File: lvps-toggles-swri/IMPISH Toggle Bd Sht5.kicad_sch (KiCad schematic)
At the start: 22 parts, among them J7 BCS-105-L-D-TE, J8 BCS-105-L-D-TE, Q25 MMBT3904Q, Q26 MMBT3906Q, Q27 ZXM61N02F, U13 BSP742T, U14 BSP452

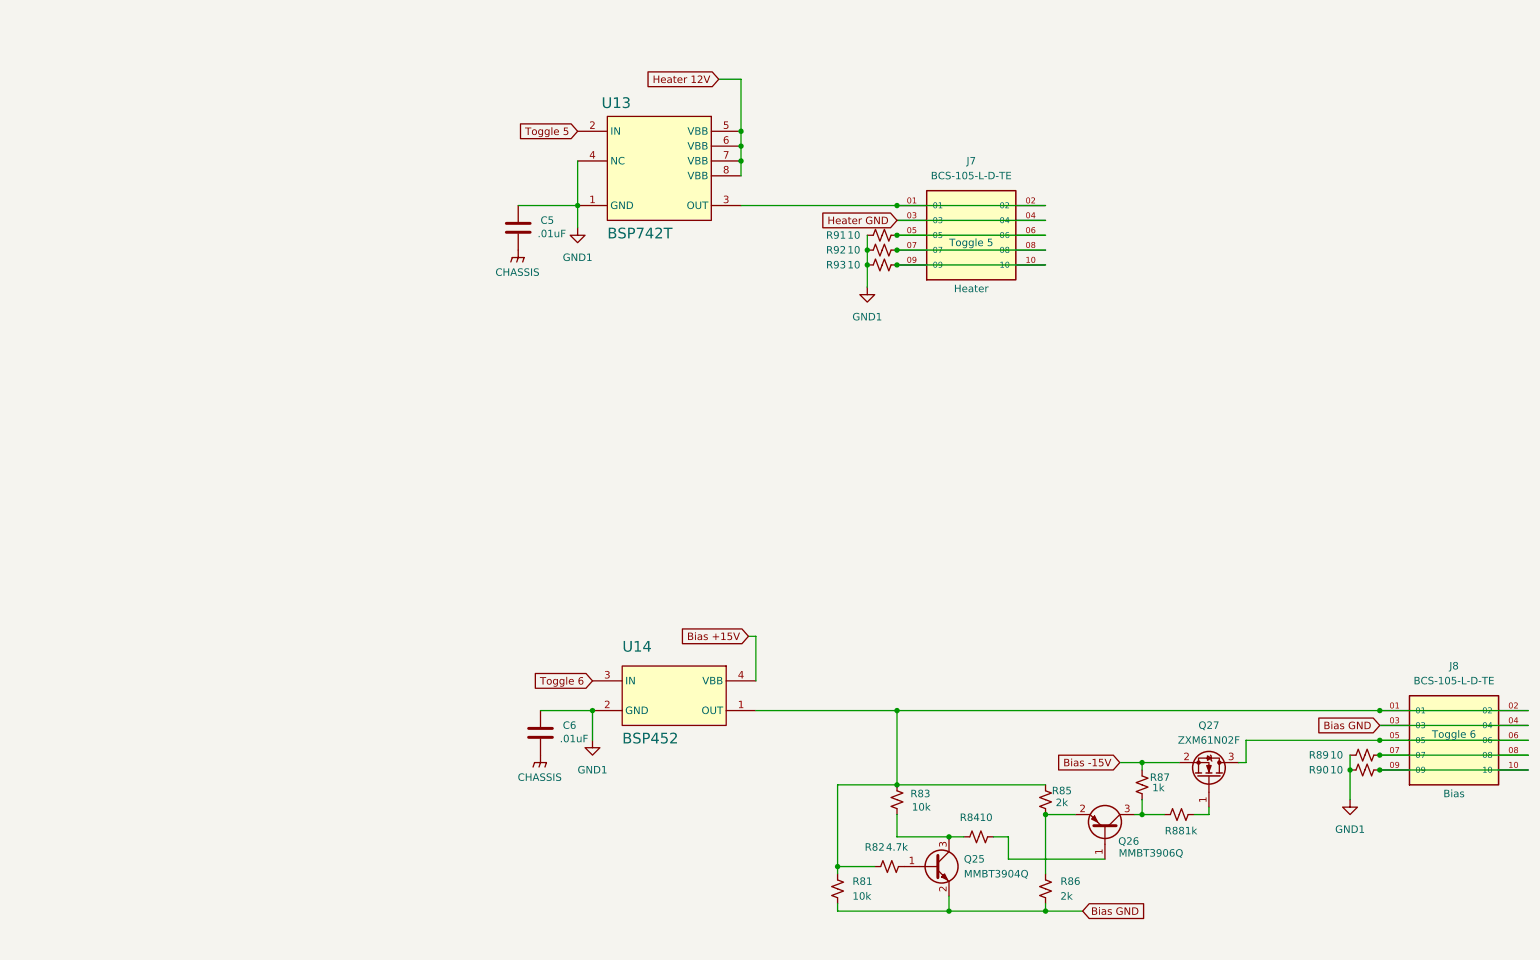
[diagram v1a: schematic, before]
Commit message: swri toggles: start one ground
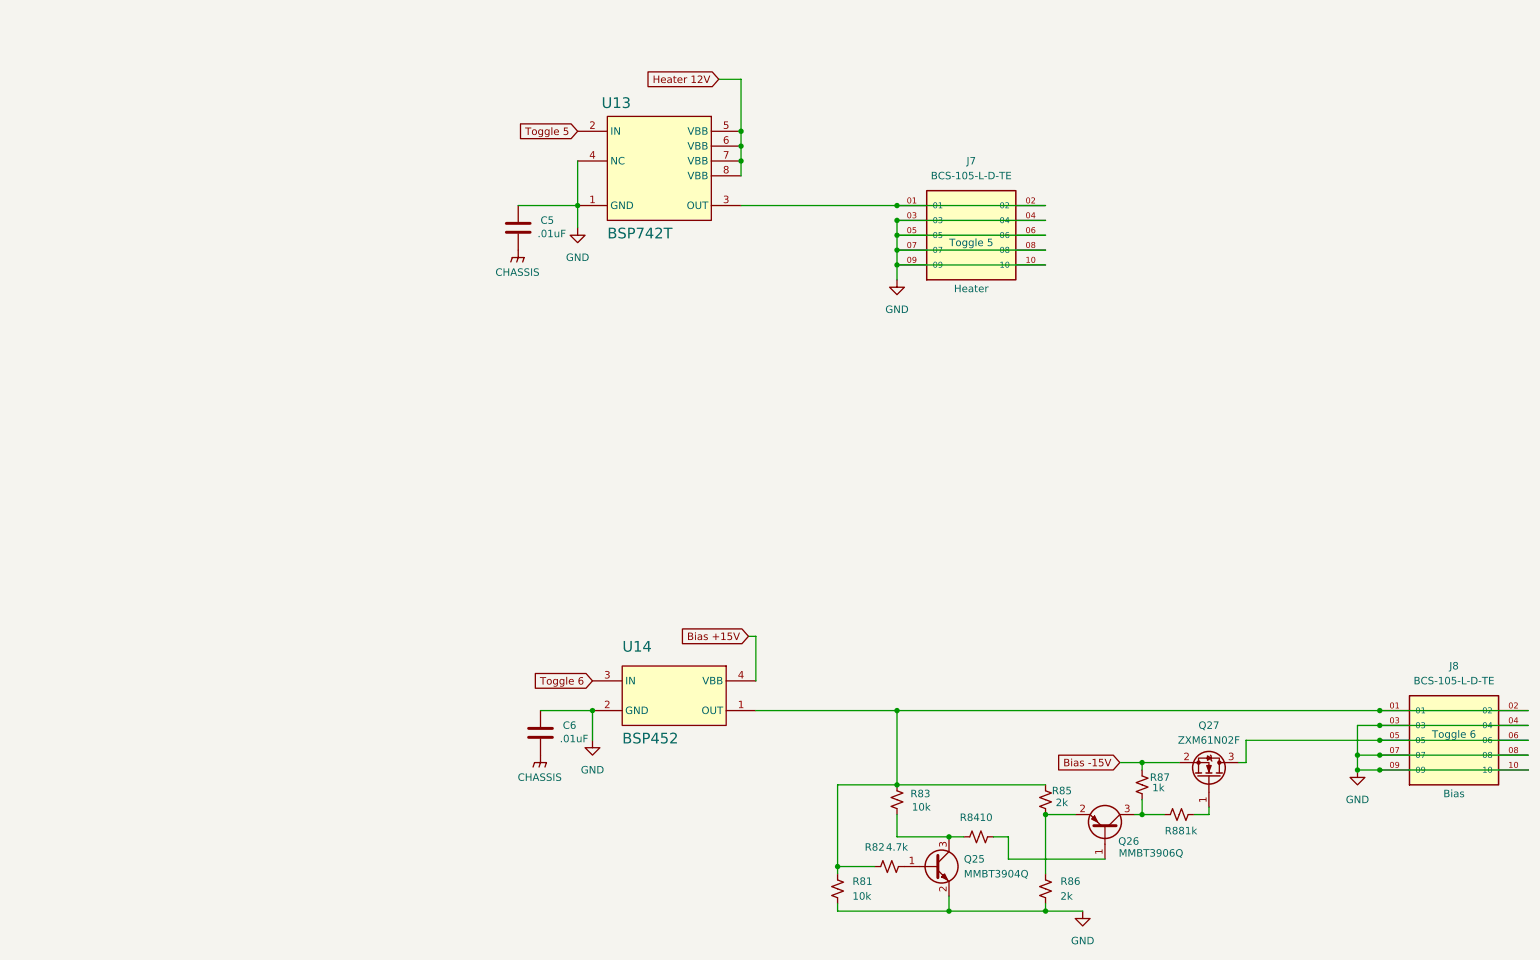
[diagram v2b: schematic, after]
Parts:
- removed R89, R90, R91, R92, R93: 10, Resistor_SMD:R_0805_2012Metric_Pad1.20x1.40mm_HandSolder, symbol Device:R_Small_US
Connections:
- net Bias GND is gone; now on net GND: J8.03, J8.04, Q25.2 (E), R81.2, R86.2
- net GND1 is gone; now on net GND: C5.2, C6.2, U13.1 (GND), U13.4 (NC), U14.2 (GND)
- net Heater GND is gone; now on net GND: J7.03, J7.04
- net GND: now reaches J8.09, J8.10
- net GND: now also J7.05, J7.06, J7.07, J7.08, J7.09, J7.10, J8.07, J8.08

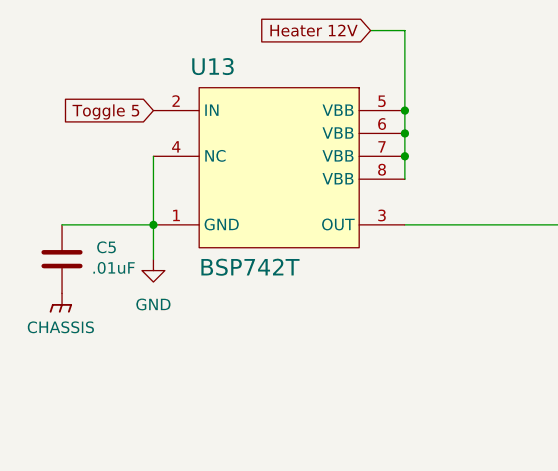
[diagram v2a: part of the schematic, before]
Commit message: swri: NC pin on toggle
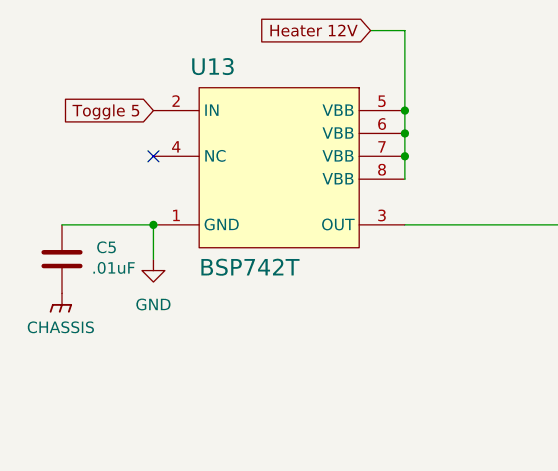
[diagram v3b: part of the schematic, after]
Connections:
- net GND: no longer U13.4 (NC)
- no-connect marks 0 -> 1
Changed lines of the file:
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@@
 		(color 0 0 0 0)
 	)
+	(no_connect
+		(at 118.11 68.58)
+	)
 	(wire
 		(pts
@@
 		)
 		(stroke
-			(width 0)
-			(type default)
-		)
-	)
-	(wire
-		(pts
-			(xy 118.11 68.58) (xy 118.11 76.2)
-		)
-		(stroke

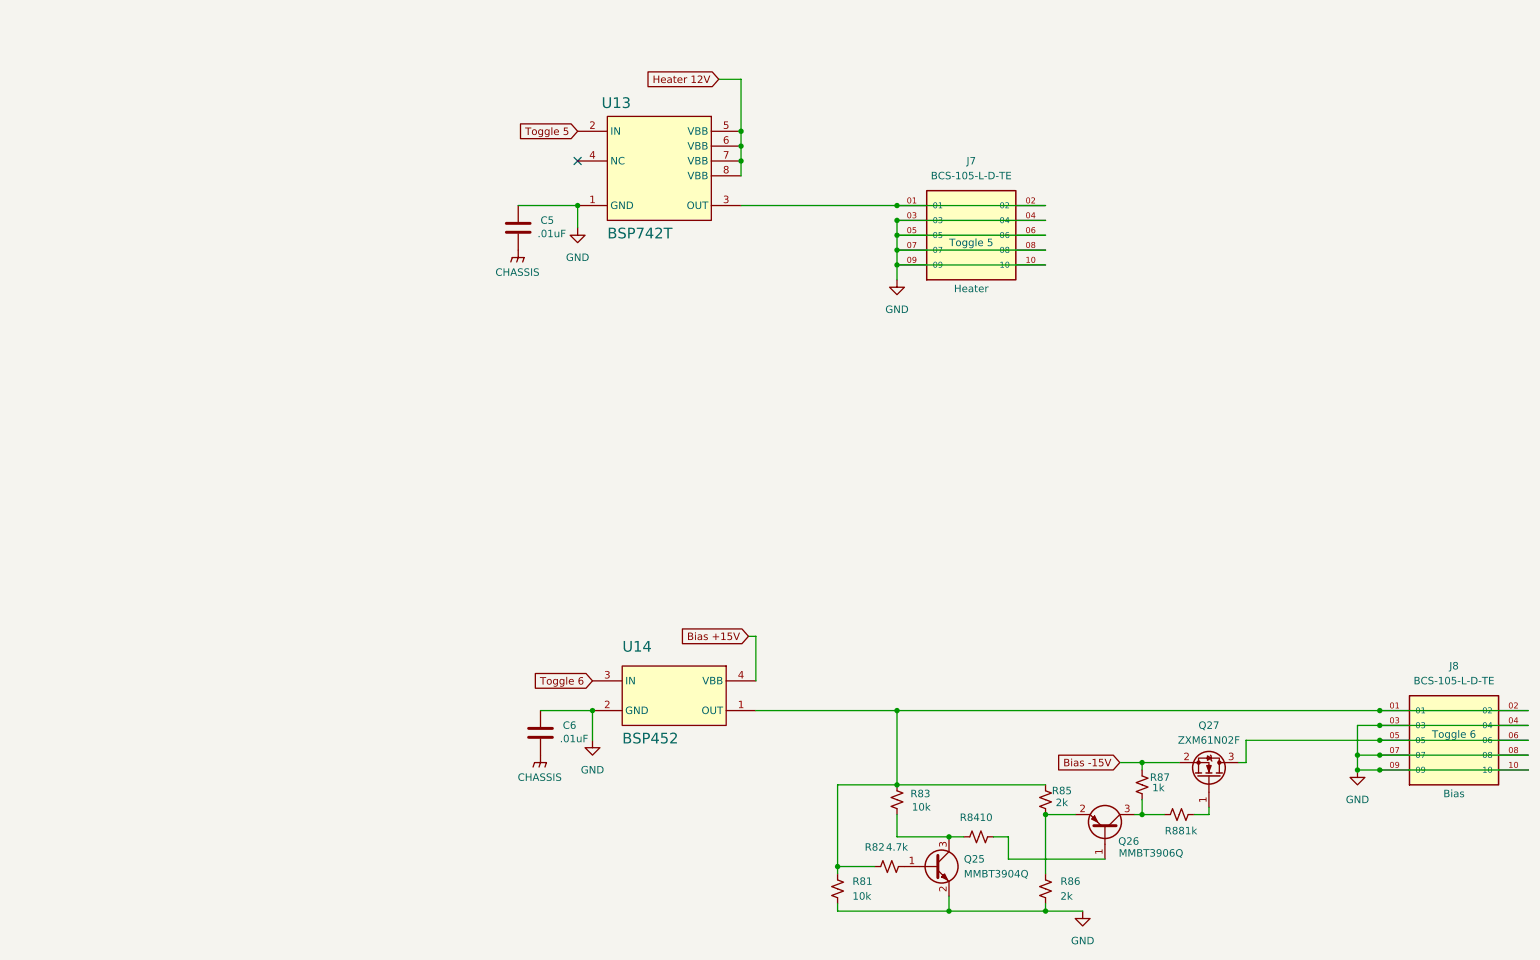
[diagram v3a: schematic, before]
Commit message: toggles
remove cremat, fix layout, add DAQBOX toggle/power line
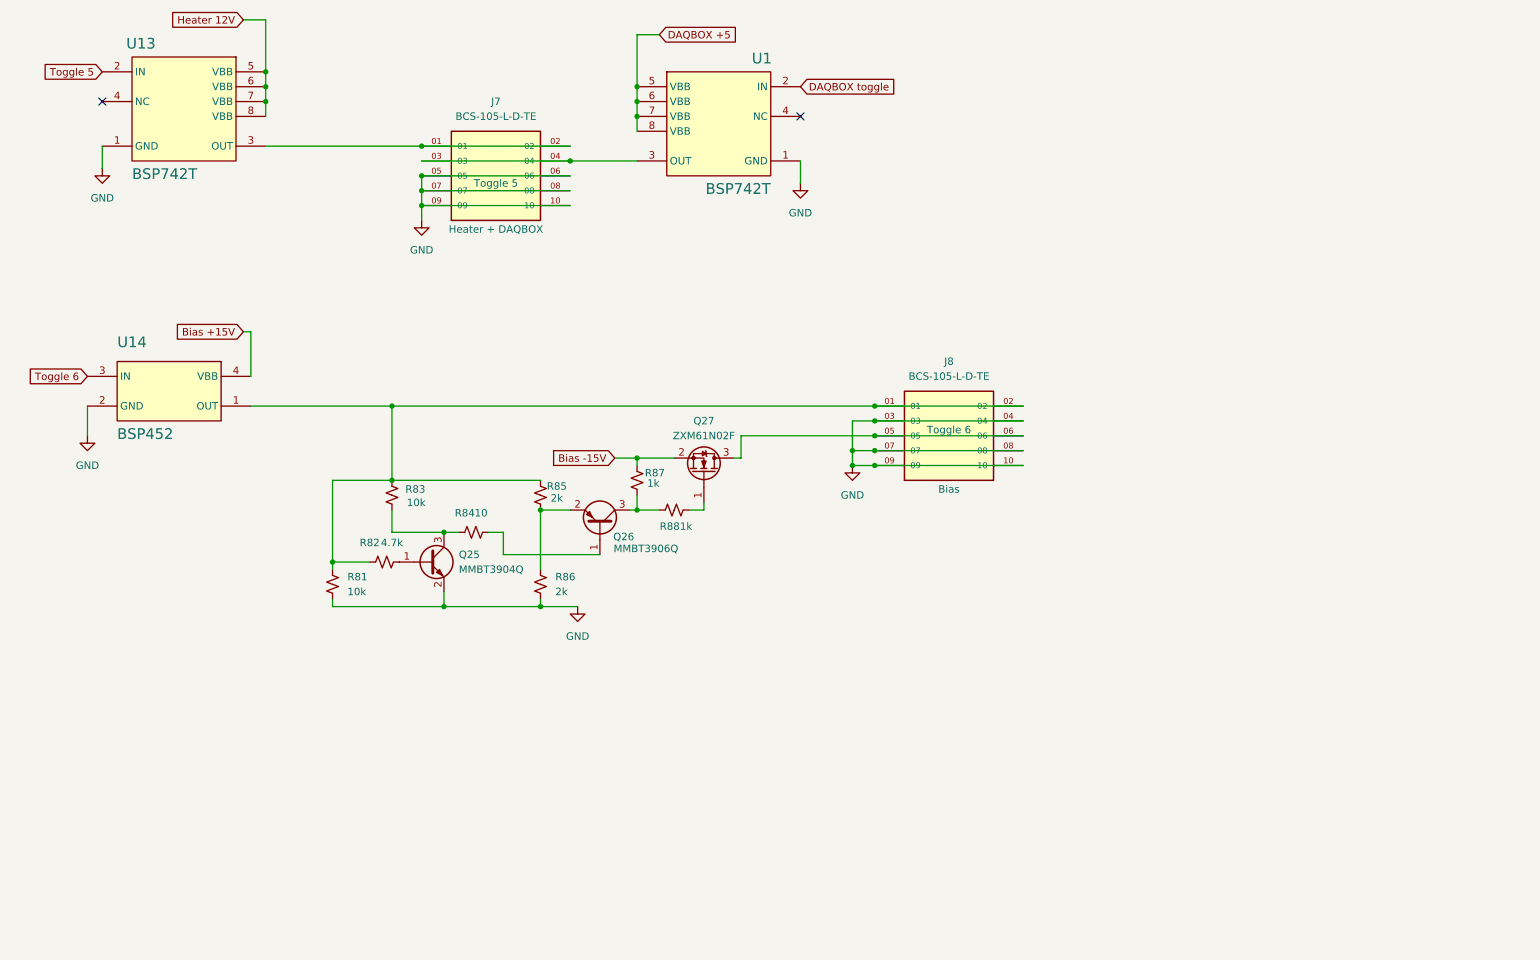
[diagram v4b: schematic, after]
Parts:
- removed C5, C6: .01uF, Capacitor_SMD:C_0805_2012Metric_Pad1.18x1.45mm_HandSolder, symbol IMPISH Toggles Library:.01uF
- added U1: BSP742T, IMPISH Toggles Library:SOIC127P600X175-8N-21, symbol IMPISH Toggles Library:BSP742T
- J7: Desc2 Heater -> Heater + DAQBOX
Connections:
- net GND: now also U1.1 (GND); no longer J7.03, J7.04
- new net: J7.03, J7.04, U1.3 (OUT)
- new net DAQBOX +5: U1.5 (VBB), U1.6 (VBB), U1.7 (VBB), U1.8 (VBB)
- new net DAQBOX toggle: U1.2 (IN)
- no-connect marks 1 -> 2
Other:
- moved on the sheet: J7, J8, Q25, Q26, Q27, R81, R82, R83, R84, R85, R86, R87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
